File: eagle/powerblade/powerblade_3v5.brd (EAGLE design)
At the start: 25.4 x 25.4 mm, 78 parts, among them J1 JTAG_14PIN_IDC-ND, J2 AC_INFINAL, J4 TC2030-JLINK-NL, Q1 NTS4173, Q4 2SK1829, U1 TPS62122, U2 MCP6V3, U3 MSP430FR5738, U4 NRF51822QF, U6 MAX9910, U7 OPA2369, X1 16MHz, X3 32.768kHz, Y1 UREACH_XTEND

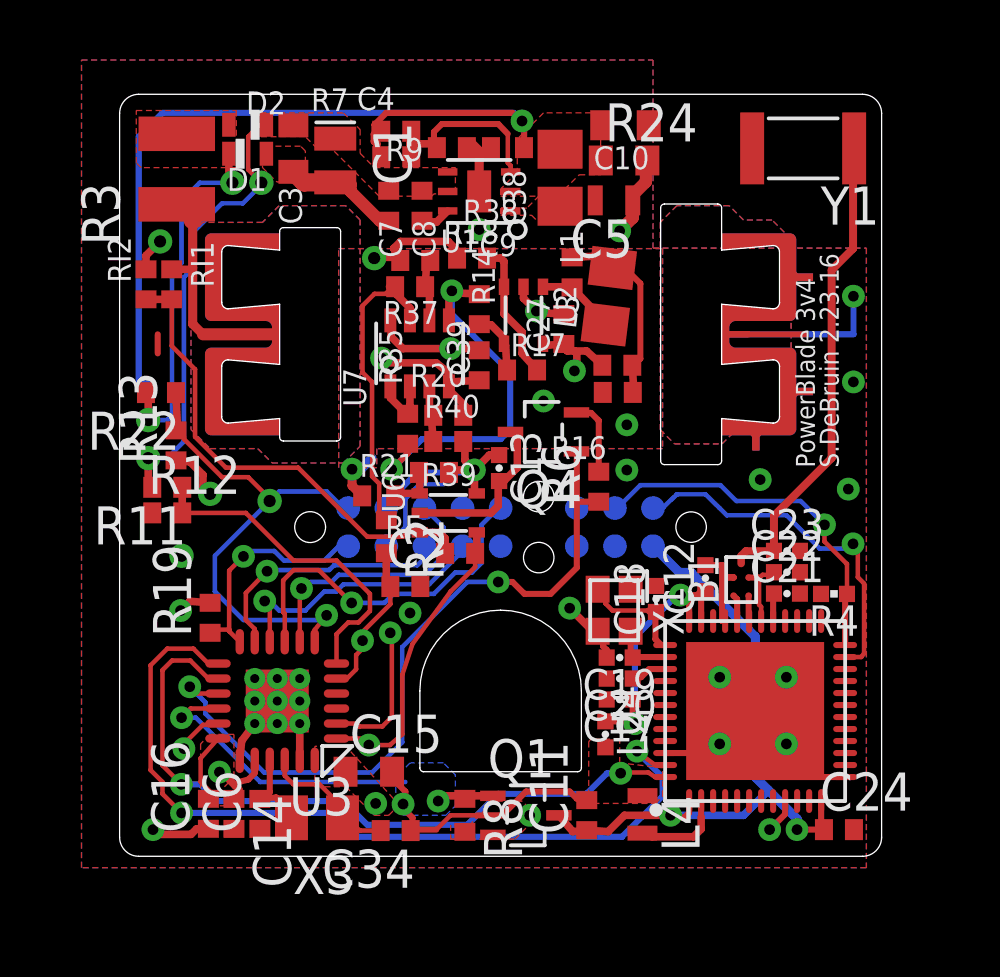
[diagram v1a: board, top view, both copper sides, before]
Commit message: moved capacitors and updated antenna
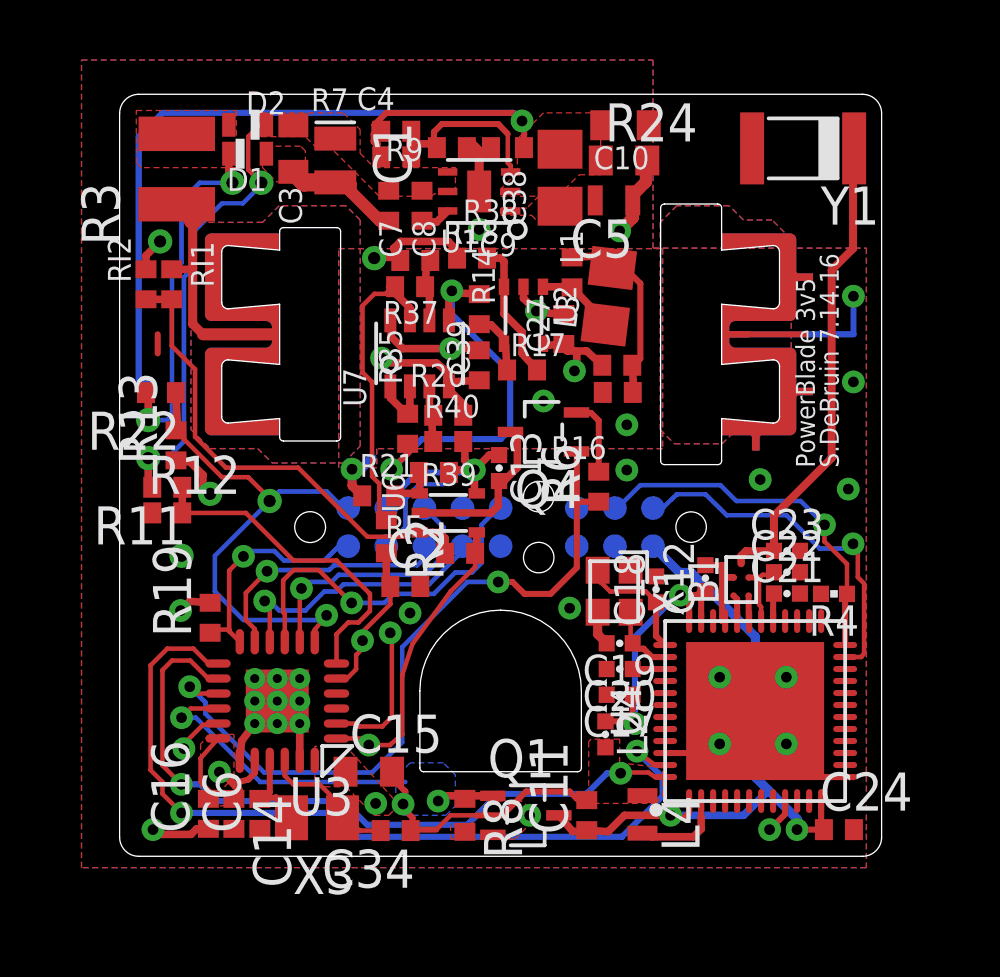
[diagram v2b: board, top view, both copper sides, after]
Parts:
- moved X1 0.63 mm to (3.78, -8.56)
- moved C19 0.48 mm to (3.97, -10.3)
- moved C18 0.32 mm to (5.18, -8.50)
- moved C20 0.32 mm to (3.97, -11.2)
- moved C17 0.16 mm to (3.97, -12.0)
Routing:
- net GND: track 52.2 -> 51.1 mm
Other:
- board text added: "1"
- board text added: "PowerBlade 3v5"
- board text added: "S.DeBruin 7.14.16"
- board text removed: "PowerBlade 3v4"
- board text removed: "S.DeBruin 2.23.16"
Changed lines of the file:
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@@
 <grid distance="25" unitdist="mil" unit="mil" style="lines" multiple="1" display="no" altdistance="3.125" altunitdist="mil" altunit="mil"/>
 <layers>
-<layer number="1" name="Top" color="4" fill="1" visible="no" active="yes"/>
-<layer number="2" name="Route2" color="1" fill="3" visible="no" active="yes"/>
+<layer number="1" name="Top" color="4" fill="1" visible="yes" active="yes"/>
+<layer number="2" name="Route2" color="1" fill="3" visible="yes" active="yes"/>
 <layer number="3" name="Route3" color="4" fill="3" visible="no" active="no"/>
 <layer number="4" name="Route4" color="1" fill="4" visible="no" active="no"/>
@@
 <layer number="13" name="Route13" color="4" fill="5" visible="no" active="no"/>
 <layer number="14" name="Route14" color="1" fill="6" visible="no" active="no"/>
-<layer number="15" name="Route15" color="4" fill="6" visible="no" active="yes"/>
+<layer number="15" name="Route15" color="4" fill="6" visible="yes" active="yes"/>
 <layer number="16" name="Bottom" color="1" fill="1" visible="yes" active="yes"/>
 <layer number="17" name="Pads" color="2" fill="1" visible="yes" active="yes"/>
@@
 <wire x1="5.207" y1="8.001" x2="5.207" y2="3.0226" width="0" layer="48"/>
 <wire x1="5.207" y1="3.0226" x2="12.7" y2="3.0226" width="0" layer="48"/>
-<text x="10.4775" y="-4.445" size="0.635" layer="21" rot="R90">PowerBlade 3v4</text>
-<text x="11.27125" y="-4.445" size="0.635" layer="21" rot="R90">S.DeBruin 2.23.16</text>
+<text x="10.4775" y="-4.445" size="0.635" layer="21" rot="R90">PowerBlade 3v5</text>
+<text x="11.27125" y="-4.445" size="0.635" layer="21" rot="R90">S.DeBruin 7.14.16</text>
 <text x="6.35" y="5.08" size="1.524" layer="22" rot="MR0">PowerBlade</text>
 <text x="3.4925" y="4.1275" size="0.762" layer="22" rot="MR0">S.DeBruin</text>
+<text x="-2.143125" y="2.54" size="1.778" layer="22" rot="MR0">1</text>
 </plain>
 <attributes>
@@
 <attribute name="DIGIKEY" value="587-1521-1-ND" x="11.1125" y="7.239" size="1.778" layer="27" rot="R270" display="off"/>
 </element>
-<element name="C17" library="passives" package="0402_CAP" value="1uF" x="3.96875" y="-12.17295" rot="R180">
-<attribute name="DIGIKEY" value="1276-1513-1-ND" x="32.92475" y="-15.98295" size="1.778" layer="27" rot="R180" display="off"/>
-</element>
-<element name="X1" library="crystals" package="TXC-8Y" value="16MHz" x="3.7846" y="-9.197975" rot="R270">
-<attribute name="DIGIKEY" value="887-2003-1-ND" x="-4.5974" y="15.948025" size="1.778" layer="27" rot="R270" display="off"/>
-</element>
-<element name="C18" library="passives" package="0402_CAP" value="12pF" x="5.1816" y="-8.82015" rot="R90">
-<attribute name="DIGIKEY" value="490-6197-1-ND" x="12.8016" y="-31.68015" size="1.778" layer="27" rot="R90" display="off"/>
-</element>
-<element name="C19" library="passives" package="0402_CAP" value="12pF" x="3.96875" y="-10.77595" rot="R180">
-<attribute name="DIGIKEY" value="490-6197-1-ND" x="31.40075" y="0.65405" size="1.778" layer="27" rot="R180" display="off"/>
-</element>
-<element name="C20" library="passives" package="0402_CAP" value="1nF" x="3.96875" y="-11.47445" rot="R180">
-<attribute name="DIGIKEY" value="490-1303-1-ND" x="10.06475" y="-3.85445" size="1.778" layer="27" rot="R180" display="off"/>
+<element name="C17" library="passives" package="0402_CAP" value="1uF" x="3.96875" y="-12.0142" rot="R180">
+<attribute name="DIGIKEY" value="1276-1513-1-ND" x="32.92475" y="-15.8242" size="1.778" layer="27" rot="R180" display="off"/>
+</element>
+<element name="X1" library="crystals" package="TXC-8Y" value="16MHz" x="3.7846" y="-8.562975" rot="R270">
+<attribute name="DIGIKEY" value="887-2003-1-ND" x="-4.5974" y="16.583025" size="1.778" layer="27" rot="R270" display="off"/>
+</element>
+<element name="C18" library="passives" package="0402_CAP" value="12pF" x="5.1816" y="-8.50265" rot="R90">
+<attribute name="DIGIKEY" value="490-6197-1-ND" x="12.8016" y="-31.36265" size="1.778" layer="27" rot="R90" display="off"/>
+</element>
+<element name="C19" library="passives" package="0402_CAP" value="12pF" x="3.96875" y="-10.2997" rot="R180">
+<attribute name="DIGIKEY" value="490-6197-1-ND" x="31.40075" y="1.1303" size="1.778" layer="27" rot="R180" display="off"/>
+</element>
+<element name="C20" library="passives" package="0402_CAP" value="1nF" x="3.96875" y="-11.15695" rot="R180">
+<attribute name="DIGIKEY" value="490-1303-1-ND" x="10.06475" y="-3.53695" size="1.778" layer="27" rot="R180" display="off"/>
 </element>
 <element name="C21" library="passives" package="0402_CAP" value="47nF" x="9.54405" y="-8.64235">
@@
 <wire x1="3.4925" y1="-12.90193125" x2="4.39928125" y2="-12.90193125" width="0.2032" layer="1"/>
 <wire x1="4.39928125" y1="-12.90193125" x2="4.47675" y2="-12.9794" width="0.2032" layer="1"/>
-<wire x1="4.40181875" y1="-12.17295" x2="4.40181875" y2="-12.90446875" width="0.2032" layer="1"/>
+<wire x1="4.40181875" y1="-12.0142" x2="4.40181875" y2="-12.90446875" width="0.2032" layer="1"/>
 <wire x1="4.40181875" y1="-12.90446875" x2="4.47675" y2="-12.9794" width="0.2032" layer="1"/>
 <wire x1="6.6675" y1="-8.5725" x2="6.54685" y2="-8.69315" width="0.2032" layer="1"/>
@@
 <contactref element="X1" pad="1"/>
 <contactref element="U4" pad="37"/>
-<wire x1="5.4836" y1="-10.357125" x2="5.3565" y2="-10.357125" width="0.2032" layer="1"/>
-<wire x1="5.3565" y1="-10.357125" x2="5.159375" y2="-10.16" width="0.2032" layer="1"/>
-<wire x1="5.159375" y1="-10.16" x2="5.159375" y2="-9.27544375" width="0.2032" layer="1"/>
-<wire x1="5.159375" y1="-9.27544375" x2="5.1816" y2="-9.25321875" width="0.2032" layer="1"/>
-<wire x1="5.1816" y1="-9.25321875" x2="4.96696875" y2="-9.25321875" width="0.2032" layer="1"/>
-<wire x1="4.96696875" y1="-9.25321875" x2="4.92125" y2="-9.2075" width="0.2032" layer="1"/>
-<wire x1="4.92125" y1="-9.2075" x2="3.730625" y2="-9.2075" width="0.1524" layer="1"/>
-<wire x1="3.730625" y1="-9.2075" x2="3.4925" y2="-8.969375" width="0.1524" layer="1"/>
-<wire x1="3.4925" y1="-8.969375" x2="3.4925" y2="-8.755875" width="0.1524" layer="1"/>
-<wire x1="3.4925" y1="-8.755875" x2="3.2346" y2="-8.497975" width="0.1524" layer="1"/>
+<wire x1="3.2346" y1="-7.862975" x2="3.33375" y2="-7.962125" width="0.2032" layer="1"/>
+<wire x1="3.33375" y1="-7.962125" x2="3.33375" y2="-8.255" width="0.2032" layer="1"/>
+<wire x1="3.33375" y1="-8.255" x2="3.65125" y2="-8.5725" width="0.1524" layer="1"/>
+<wire x1="3.65125" y1="-8.5725" x2="4.841875" y2="-8.5725" width="0.1524" layer="1"/>
+<wire x1="5.12571875" y1="-8.93571875" x2="5.1816" y2="-8.93571875" width="0.2032" layer="1"/>
+<wire x1="4.841875" y1="-8.5725" x2="5.1816" y2="-8.912225" width="0.1524" layer="1"/>
+<wire x1="5.1816" y1="-8.912225" x2="5.1816" y2="-8.93571875" width="0.1524" layer="1"/>
+<wire x1="5.1816" y1="-8.93571875" x2="5.1816" y2="-10.055125" width="0.2032" layer="1"/>
+<wire x1="5.1816" y1="-10.055125" x2="5.4836" y2="-10.357125" width="0.2032" layer="1"/>
 </signal>
 <signal name="N$17">
@@
 <contactref element="C19" pad="1"/>
 <contactref element="U4" pad="38"/>
-<wire x1="5.4836" y1="-10.757125" x2="4.42064375" y2="-10.757125" width="0.2032" layer="1"/>
-<wire x1="4.42064375" y1="-10.757125" x2="4.40181875" y2="-10.77595" width="0.2032" layer="1"/>
-<wire x1="4.3346" y1="-9.897975" x2="4.3346" y2="-10.67108125" width="0.2032" layer="1"/>
-<wire x1="4.3346" y1="-10.67108125" x2="4.42064375" y2="-10.757125" width="0.2032" layer="1"/>
+<wire x1="5.4836" y1="-10.757125" x2="5.042125" y2="-10.757125" width="0.2032" layer="1"/>
+<wire x1="5.042125" y1="-10.757125" x2="4.7625" y2="-10.4775" width="0.2032" layer="1"/>
+<wire x1="4.7625" y1="-10.4775" x2="4.57961875" y2="-10.4775" width="0.2032" layer="1"/>
+<wire x1="4.57961875" y1="-10.4775" x2="4.40181875" y2="-10.2997" width="0.2032" layer="1"/>
+<wire x1="4.40181875" y1="-10.2997" x2="4.3346" y2="-10.23248125" width="0.1524" layer="1"/>
+<wire x1="4.3346" y1="-10.23248125" x2="4.3346" y2="-9.262975" width="0.1524" layer="1"/>
 </signal>
 <signal name="N$18">
 <contactref element="U4" pad="39"/>
 <contactref element="C20" pad="1"/>
-<wire x1="5.4836" y1="-11.157125" x2="4.956" y2="-11.157125" width="0.2032" layer="1"/>
-<wire x1="4.956" y1="-11.157125" x2="4.683125" y2="-11.43" width="0.2032" layer="1"/>
-<wire x1="4.683125" y1="-11.43" x2="4.44626875" y2="-11.43" width="0.2032" layer="1"/>
-<wire x1="4.44626875" y1="-11.43" x2="4.40181875" y2="-11.47445" width="0.2032" layer="1"/>
+<wire x1="5.4836" y1="-11.157125" x2="4.40181875" y2="-11.157125" width="0.2032" layer="1"/>
+<wire x1="4.40181875" y1="-11.157125" x2="4.40181875" y2="-11.15695" width="0.2032" layer="1"/>
 </signal>
 <signal name="N$19">
@@
 <contactref element="X1" pad="4"/>
 <contactref element="X1" pad="2"/>
-<wire x1="3.53568125" y1="-10.77595" x2="3.53568125" y2="-10.52068125" width="0.2032" layer="1"/>
-<wire x1="3.53568125" y1="-10.52068125" x2="3.413125" y2="-10.398125" width="0.2032" layer="1"/>
-<wire x1="3.413125" y1="-10.398125" x2="3.413125" y2="-10.0765" width="0.2032" layer="1"/>
-<wire x1="3.413125" y1="-10.0765" x2="3.2346" y2="-9.897975" width="0.2032" layer="1"/>
 <via x="2.301875" y="-9.128125" extent="1-16" drill="0.3556"/>
-<wire x1="3.2346" y1="-9.897975" x2="3.071725" y2="-9.897975" width="0.254" layer="1"/>
-<wire x1="3.071725" y1="-9.897975" x2="2.301875" y2="-9.128125" width="0.254" layer="1"/>
 <contactref element="C17" pad="2"/>
 <contactref element="C24" pad="2"/>
@@
 <wire x1="-4.024375" y1="3.78625" x2="-3.730625" y2="3.78625" width="0.4064" layer="1"/>
 <wire x1="7.493" y1="0" x2="10.16" y2="0" width="0.2032" layer="1"/>
+<wire x1="3.2346" y1="-9.262975" x2="3.2346" y2="-9.99861875" width="0.3048" layer="1"/>
+<wire x1="3.2346" y1="-9.99861875" x2="3.53568125" y2="-10.2997" width="0.3048" layer="1"/>
 </signal>
 <signal name="TEMP">
